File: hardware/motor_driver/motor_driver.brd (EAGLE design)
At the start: 100 x 80 mm, 64 parts

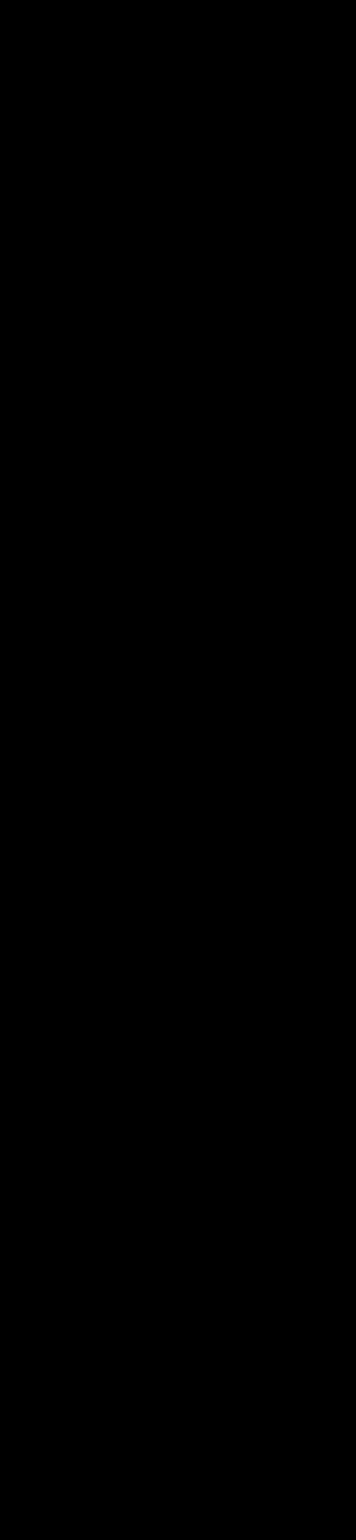
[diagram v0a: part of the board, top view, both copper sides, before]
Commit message: Full Motor Driver updates and first in depth review of the board
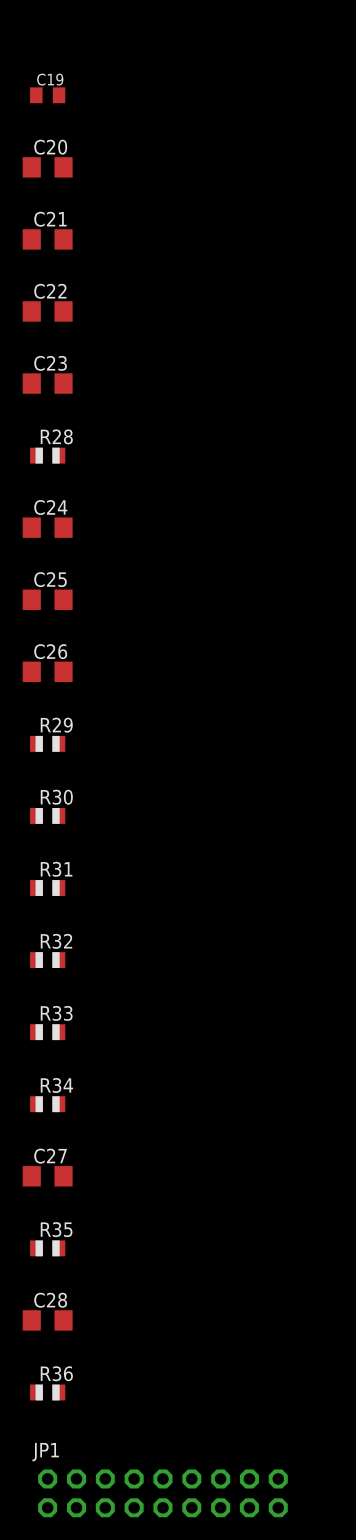
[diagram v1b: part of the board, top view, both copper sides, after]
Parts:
- added C19: 15n, adafruit:C0805K
- added C20, C24, C25, C26: 0.1u, adafruit:C1206
- added C21, C22: 4.7u, adafruit:C1206
- added C23: 10n, adafruit:C1206
- added C27, C28: 1n, adafruit:C1206
- added JP1: (no value), adafruit:2X09-CLEANBIG
- added R28: 3.3, adafruit:R0805
- added R29, R30, R31, R32, R33, R34: 4.7k, adafruit:R0805
- added R35, R36: 10m, adafruit:R0805
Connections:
- net VCC renamed REF
- removed net G4: R22.2, U$3.G
- removed net G5: R23.2, U$2.G
- removed net G6: R24.2, U$1.G
- removed net M_L4: R27.1
- removed net M_L5: R26.1
- removed net M_L6: R25.1
- removed net PVDD(2): U$7.P$35
- removed net PVDD1: C7.2, C9.2, U$7.P$27
- removed net PWGRD: R10.1
- removed net SA_A: U$7.P$54
- new net GH_A: R29.2, U$7.P$55
- new net GH_B: R30.2, U$7.P$50
- new net GH_C: R31.2, U$7.P$45
- new net GL_A: R32.2, U$7.P$53
- new net GL_B: R33.2, U$7.P$48
- new net GL_C: R34.2, U$7.P$43
- new net N$15: C7.2, C8.2, C9.2
- new net N$16: U$7.P$31
- new net N$3: C4.1, R12.1
- new net N$4: R22.2, R25.1
- new net N$5: R23.2, R26.1
- new net N$6: R24.2, R27.1
- new net N$7: C23.1, R28.1
- new net N$8: C14.1, C15.1, U$7.GND
- new net PGND: C20.2, C21.2, C22.2, C23.2, C27.2, C28.2, R35.2, R36.2
- new net PVDD: C20.1, C21.1, C22.1, R28.2, U$7.P$16, U$7.P$27, U$7.P$35
- new net SH_B: C25.2
- new net SH_C: C26.2
- new net SS_TR: C19.1, U$7.P$22
- net 5V: no longer C4.1, R12.1, U$7.P$22
- net AGND: now also C13.2, C14.2, C15.2
- net BST_A: now also C24.1
- net BST_B: now also C25.1
- net BST_C: now also C26.1
- net DC_CAL: now also JP1.9
- net DVDD: no longer C15.1, U$7.GND
- net EN_BUCK: now also JP1.2
- net EN_GATE: now also JP1.1
- net G1: no longer U$6.G
- net G2: no longer U$5.G
- net G3: no longer U$4.G
- net GND: now also C19.2; no longer C13.2, C14.2, C15.2, U$7.P$31
- net H1: now also JP1.3
- net H1_LOW: now also C27.1, R35.1, U$3.S2, U$3.S3, U$3.S4
- net H1_VS: now also C24.2, U$6.S1, U$6.S2, U$6.S3, U$6.S4, U$6.S5, U$7.P$54
- net H2: now also JP1.5
- net H2_LOW: now also C28.1, R36.1, U$2.S2, U$2.S3, U$2.S4
- net H2_VS: now also U$5.S1, U$5.S2, U$5.S3, U$5.S4, U$5.S5
- net H3: now also JP1.7
- net H3_LOW: now also U$1.S2, U$1.S3, U$1.S4
- net H3_VS: now also U$4.S1, U$4.S2, U$4.S3, U$4.S4, U$4.S5
- net L1: now also JP1.4
- net L2: now also JP1.6
- net L3: now also JP1.8
- net M_H1: now also R29.1, U$6.G; no longer U$7.P$55
- net M_H2: now also R30.1, U$5.G; no longer U$7.P$50
- net M_H3: now also R31.1, U$4.G; no longer U$7.P$45
- net M_L1: now also R32.1, U$3.G; no longer U$7.P$53
- net M_L2: now also R33.1, U$2.G; no longer U$7.P$48
- net M_L3: now also R34.1, U$1.G; no longer U$7.P$43
- net PVDD2: no longer U$7.P$16
- net PWRGD: now also R10.1
- net S1: no longer U$6.S1, U$6.S5
- net S2: no longer U$5.S1, U$5.S5
- net S3: no longer U$4.S1, U$4.S5

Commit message: Pushing library updates
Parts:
- added JP2: (no value), adafruit:1X06
- JP1: device adafruit:2X09-CLEANBIG -> adafruit:1X09-BIG
- moved R33 194.9 mm to (52.1, 53.3)
- moved C27 169.7 mm to (35.6, 21.6)
- moved C28 169.7 mm to (35.6, 8.89)
- moved R34 169.7 mm to (35.6, 27.9)
- moved R35 169.7 mm to (35.6, 15.2)
- moved R36 169.7 mm to (35.6, 2.54)
- moved C25 139.7 mm to (29.2, 34.3)
- moved C26 139.7 mm to (29.2, 27.9)
- moved R29 139.7 mm to (29.2, 21.6)
- moved R30 139.7 mm to (29.2, 15.2)
- moved R31 139.7 mm to (29.2, 8.89)
- moved R32 139.7 mm to (29.2, 2.54)
- moved R26 72.2 mm to (19.1, 35.6), turned to 270 degrees
- moved JP1 68.6 mm to (-72.4, -59.7)
- moved R27 67.7 mm to (5.08, 35.6), turned to 270 degrees
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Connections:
- new net N$13: JP2.5
- new net N$14: JP2.6
- new net N$17: JP1.7
- new net N$18: JP1.8
- new net N$19: JP1.9
- net !FAULT: now also JP2.2
- net !OCTW: now also JP2.1
- net DC_CAL: no longer JP1.9
- net EN_BUCK: now also JP2.4; no longer JP1.2
- net EN_GATE: now also JP2.3; no longer JP1.1
- net H1: now also JP1.1; no longer JP1.3
- net H2: now also JP1.2; no longer JP1.5
- net H3: now also JP1.3; no longer JP1.7
- net L2: now also JP1.5; no longer JP1.6
- net L3: now also JP1.6; no longer JP1.8
